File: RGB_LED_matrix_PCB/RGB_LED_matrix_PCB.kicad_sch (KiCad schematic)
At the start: 0 parts

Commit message: Routed the matrix structure
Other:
- added sheet LED_ROW (10_LED_row/10_LED_row.kicad_sch)
- added sheet LED_ROW1 (10_LED_row/10_LED_row.kicad_sch)
- added sheet LED_ROW2 (10_LED_row/10_LED_row.kicad_sch)
- added sheet LED_ROW3 (10_LED_row/10_LED_row.kicad_sch)
- added sheet LED_ROW4 (10_LED_row/10_LED_row.kicad_sch)
- added sheet LED_ROW5 (10_LED_row/10_LED_row.kicad_sch)
- added sheet LED_ROW6 (10_LED_row/10_LED_row.kicad_sch)
- added sheet LED_ROW7 (10_LED_row/10_LED_row.kicad_sch)
- added sheet LED_ROW8 (10_LED_row/10_LED_row.kicad_sch)
- added sheet LED_ROW9 (10_LED_row/10_LED_row.kicad_sch)

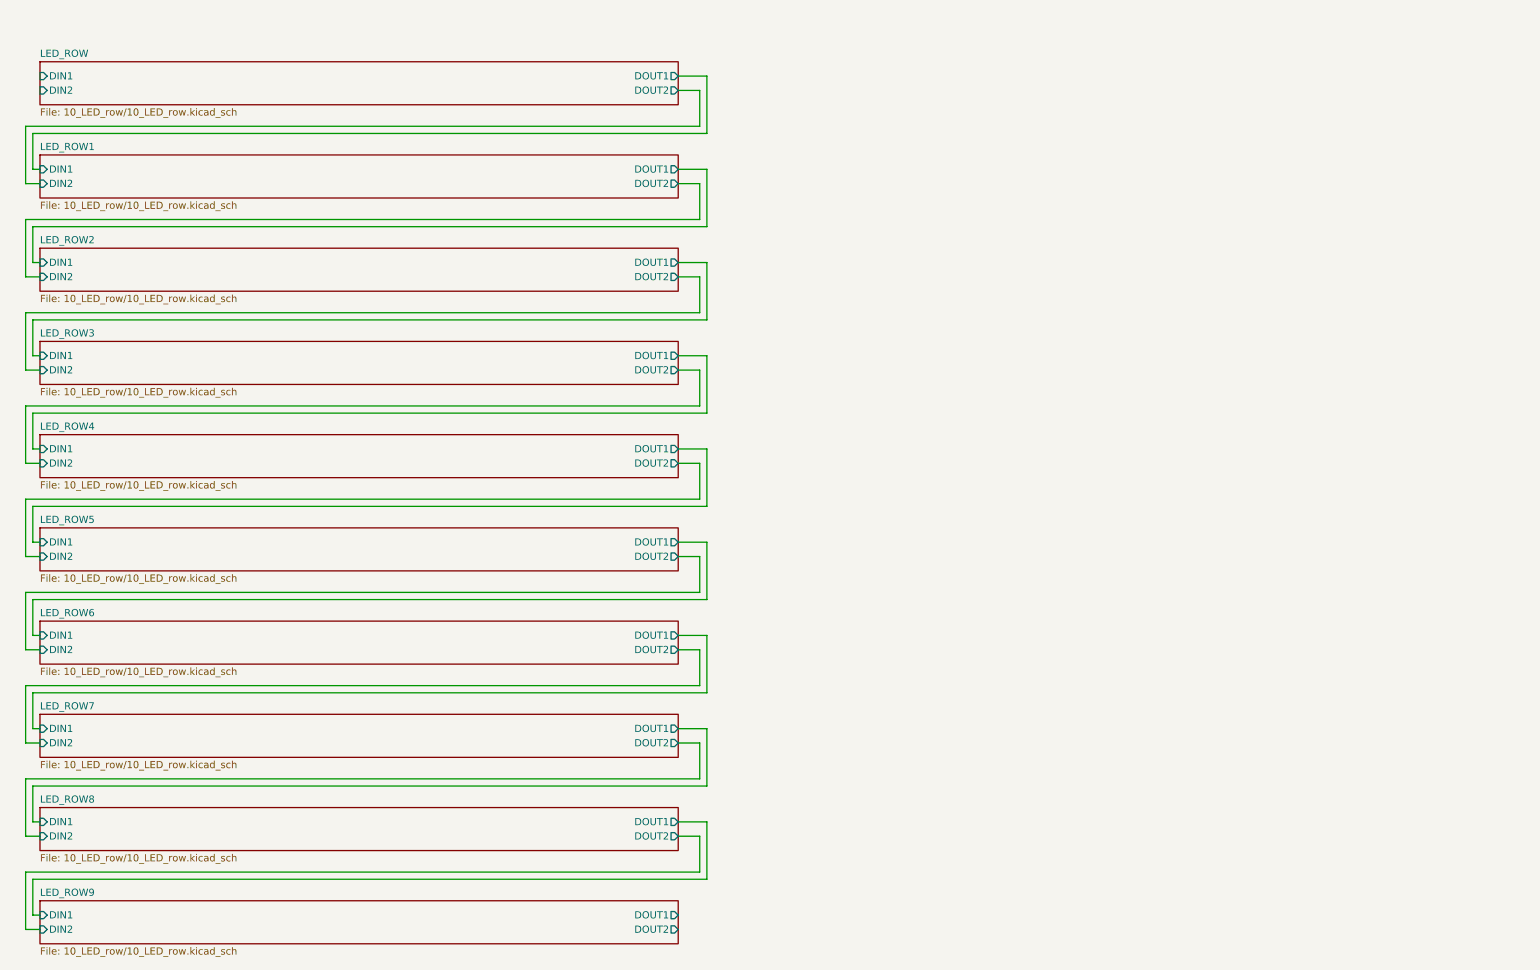
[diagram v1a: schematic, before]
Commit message: Changed LED matrix pcb design to a serpentine structure for better signal integrity. Proceeded with adding the connector and capacitors.
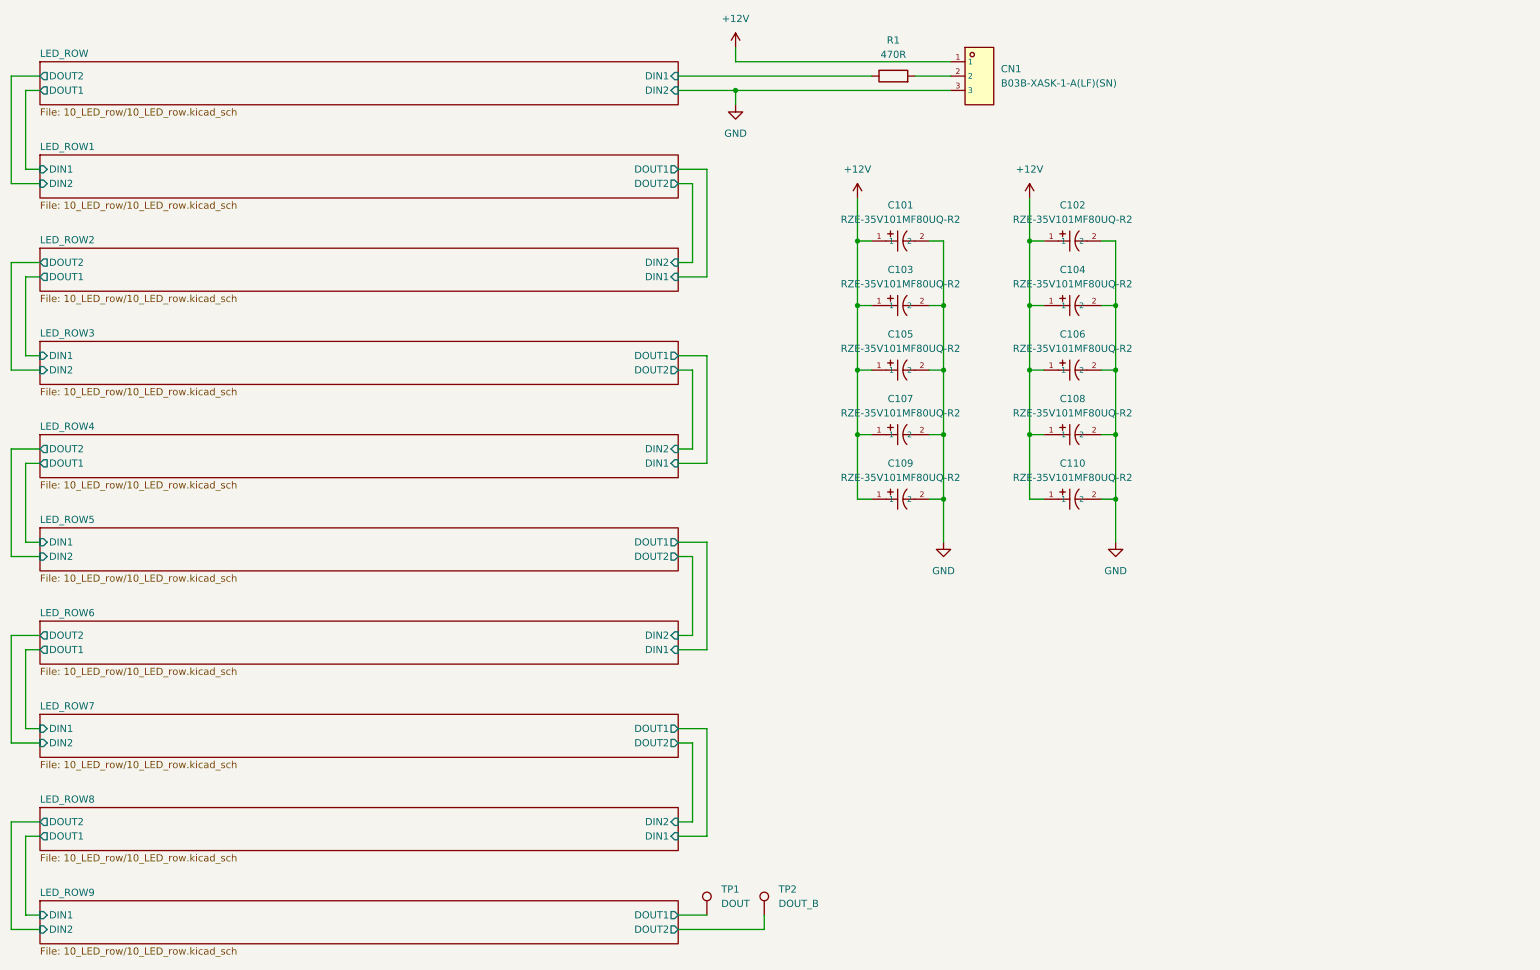
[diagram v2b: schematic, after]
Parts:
- added C101, C102, C103, C104, C105, C106, C107, C108, C109, C110: RZE-35V101MF80UQ-R2, lcsc_footprints:C19673858_CAP-SMD_BD6_3-L6_5-W6_5-LS7_2-FD_1, symbol lcsc_imported:RZE-35V101MF80UQ-R2
- added CN1: B03B-XASK-1-A(LF)(SN), lcsc_footprints:C264992_CONN-TH_B03B-XASK-1-A-LF-SN, symbol lcsc_imported:B03B-XASK-1-A(LF)(SN)
- added R1: 470R, Resistor_SMD:R_0402_1005Metric_Pad0.72x0.64mm_HandSolder, symbol Device:R
- added TP1: DOUT, TestPoint:TestPoint_Pad_D1.0mm, symbol Connector:TestPoint
- added TP2: DOUT_B, TestPoint:TestPoint_Pad_D1.0mm, symbol Connector:TestPoint
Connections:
- net LED_ROW/DIN1: now also R1.1
- net LED_ROW9/DOUT1: now also TP1.1
- net LED_ROW9/DOUT2: now also TP2.1
- new net: CN1.2, R1.2
- new net +12V: C101.1, C102.1, C103.1, C104.1, C105.1, C106.1, C107.1, C108.1, C109.1, C110.1, CN1.1
- new net GND: C101.2, C102.2, C103.2, C104.2, C105.2, C106.2, C107.2, C108.2, C109.2, C110.2, CN1.3

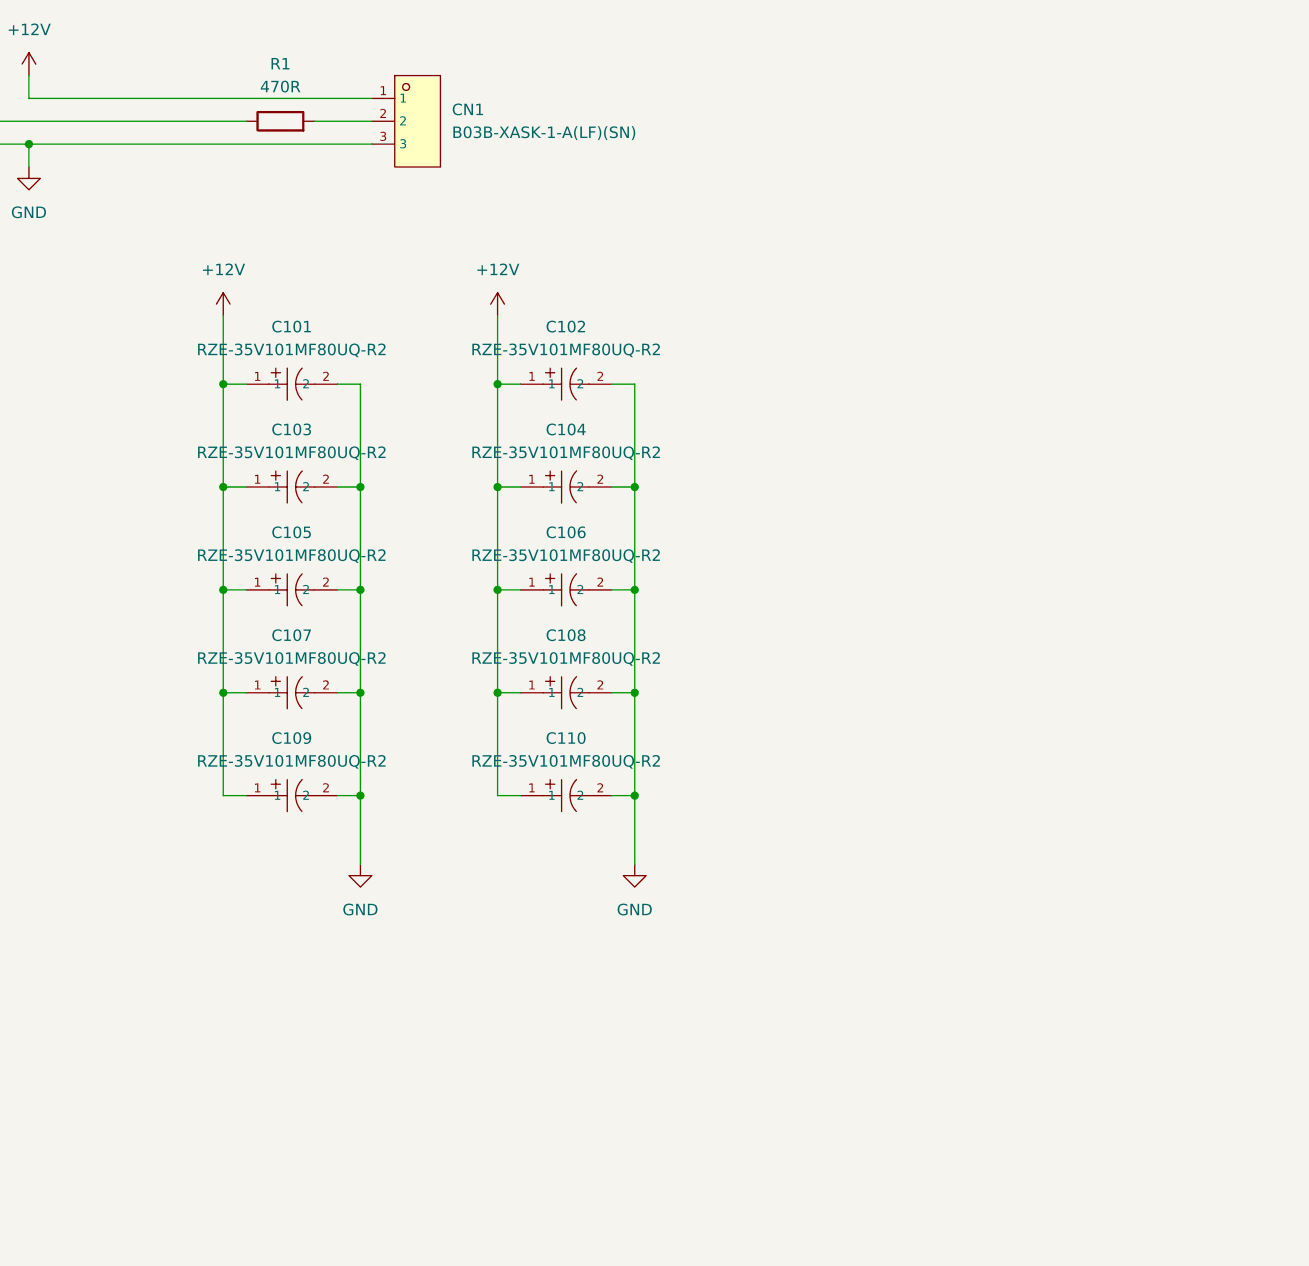
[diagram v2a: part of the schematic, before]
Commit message: Finished the LED matrix board layout - it just needs some polishing now and minor fixes
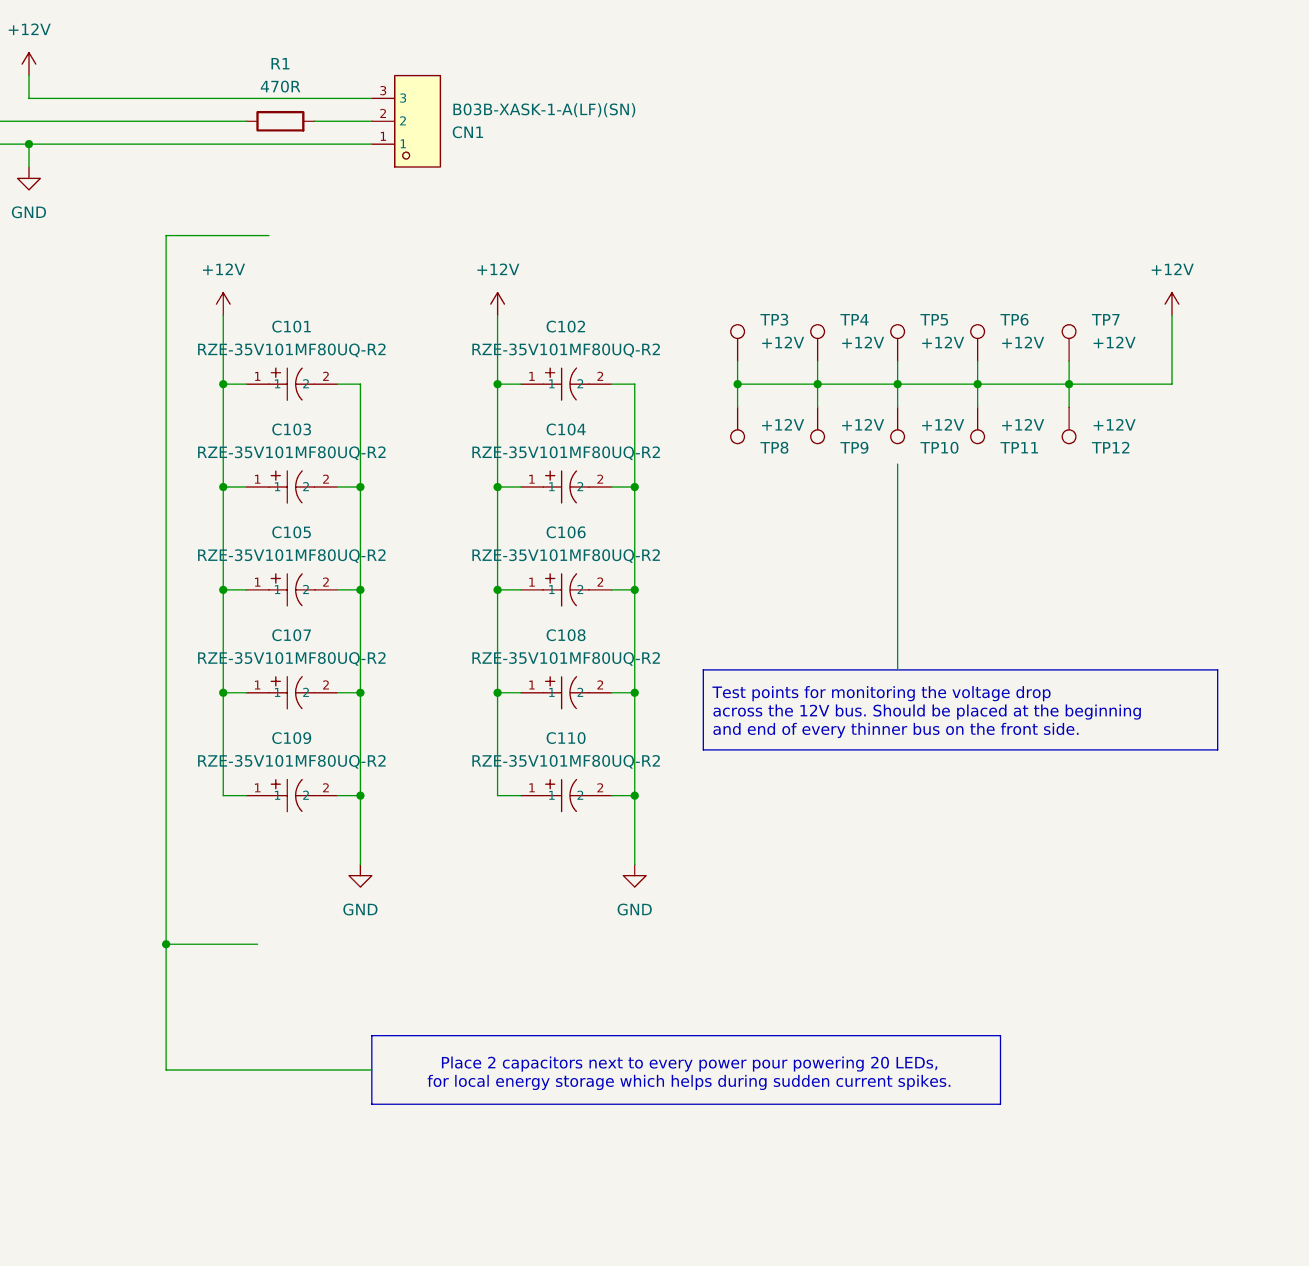
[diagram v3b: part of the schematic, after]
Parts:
- added TP10, TP11, TP12, TP3, TP4, TP5, TP6, TP7, TP8, TP9: +12V, TestPoint:TestPoint_Pad_D1.0mm, symbol Connector:TestPoint
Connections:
- net +12V: now also CN1.3, TP10.1, TP11.1, TP12.1, TP3.1, TP4.1, TP5.1, TP6.1, TP7.1, TP8.1, TP9.1; no longer CN1.1
- net GND: now also CN1.1; no longer CN1.3
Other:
- note added: "Place 2 capacitors next to every power pour powering 20 LEDs, for local energy storage which helps during sudden current spikes."
- note added: "Test points for monitoring the voltage drop across the 12V bus. Should be placed at the beginning and end of every thinner bus on the front side."
- title: (none) -> RGB LED MATRIX

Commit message: Made some slight modyfications to the RGB LED matrix layout.
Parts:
- added C111: RZE-35V101MF80UQ-R2, lcsc_footprints:C19673858_CAP-SMD_BD6_3-L6_5-W6_5-LS7_2-FD_1, symbol lcsc_imported:RZE-35V101MF80UQ-R2
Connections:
- net +12V: now also C111.1
- net GND: now also C111.2
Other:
- note added: "This is an alternate placement of the C101, mark as DNF if not needed."
- moved on the sheet: R1

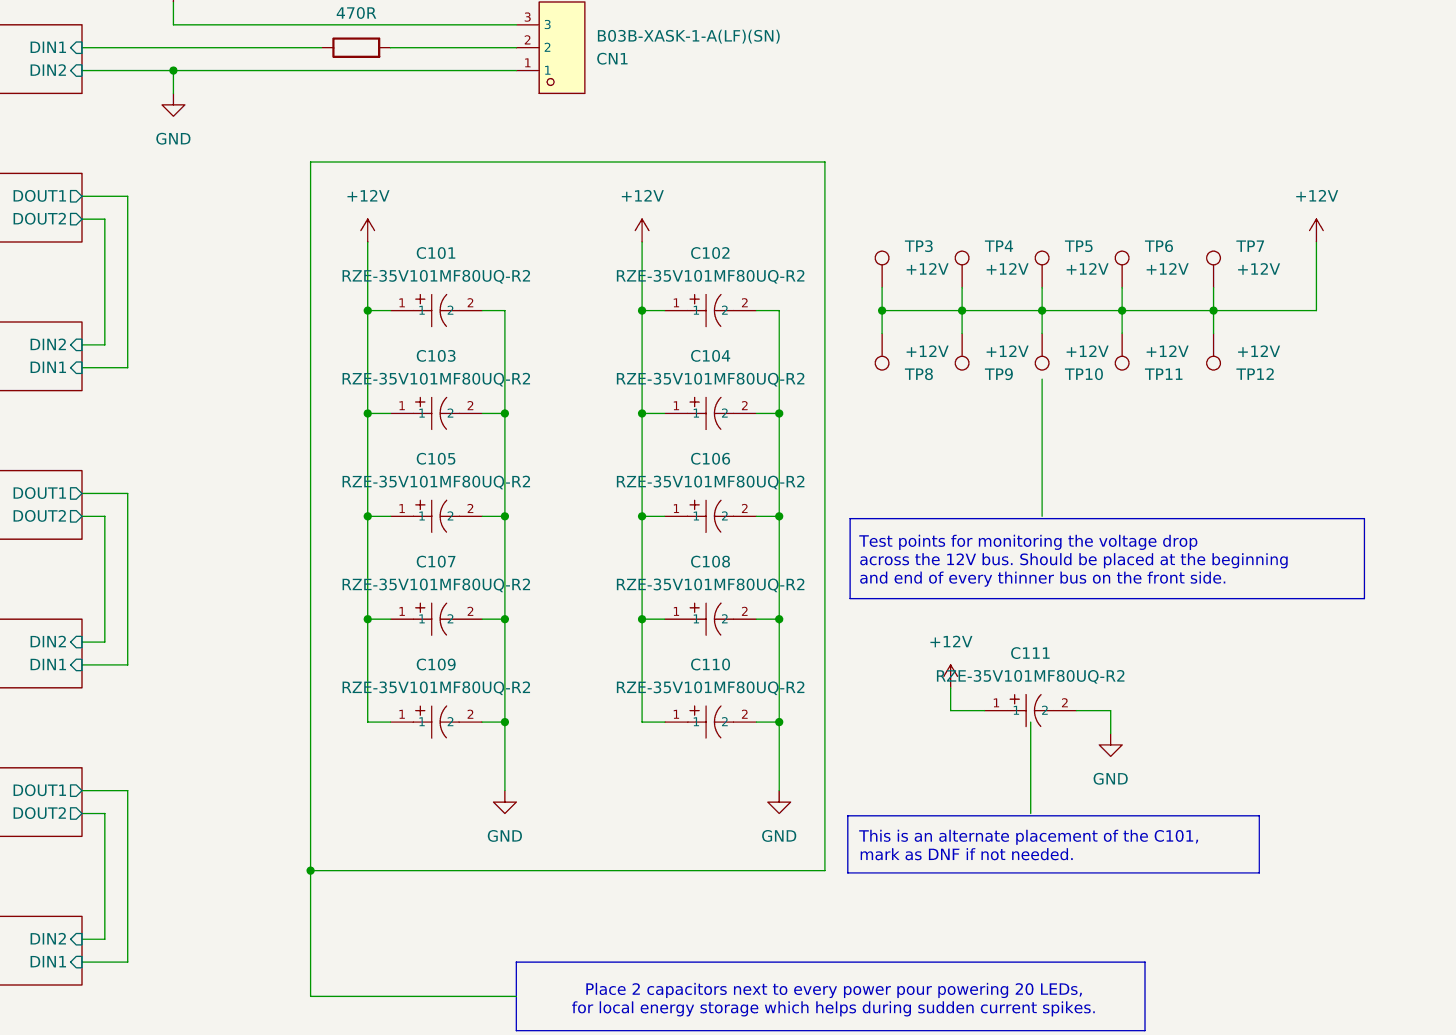
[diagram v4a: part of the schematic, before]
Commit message: Fixed silkscreen and added extra capacitor row in a new design variant in LED matrix PCB.
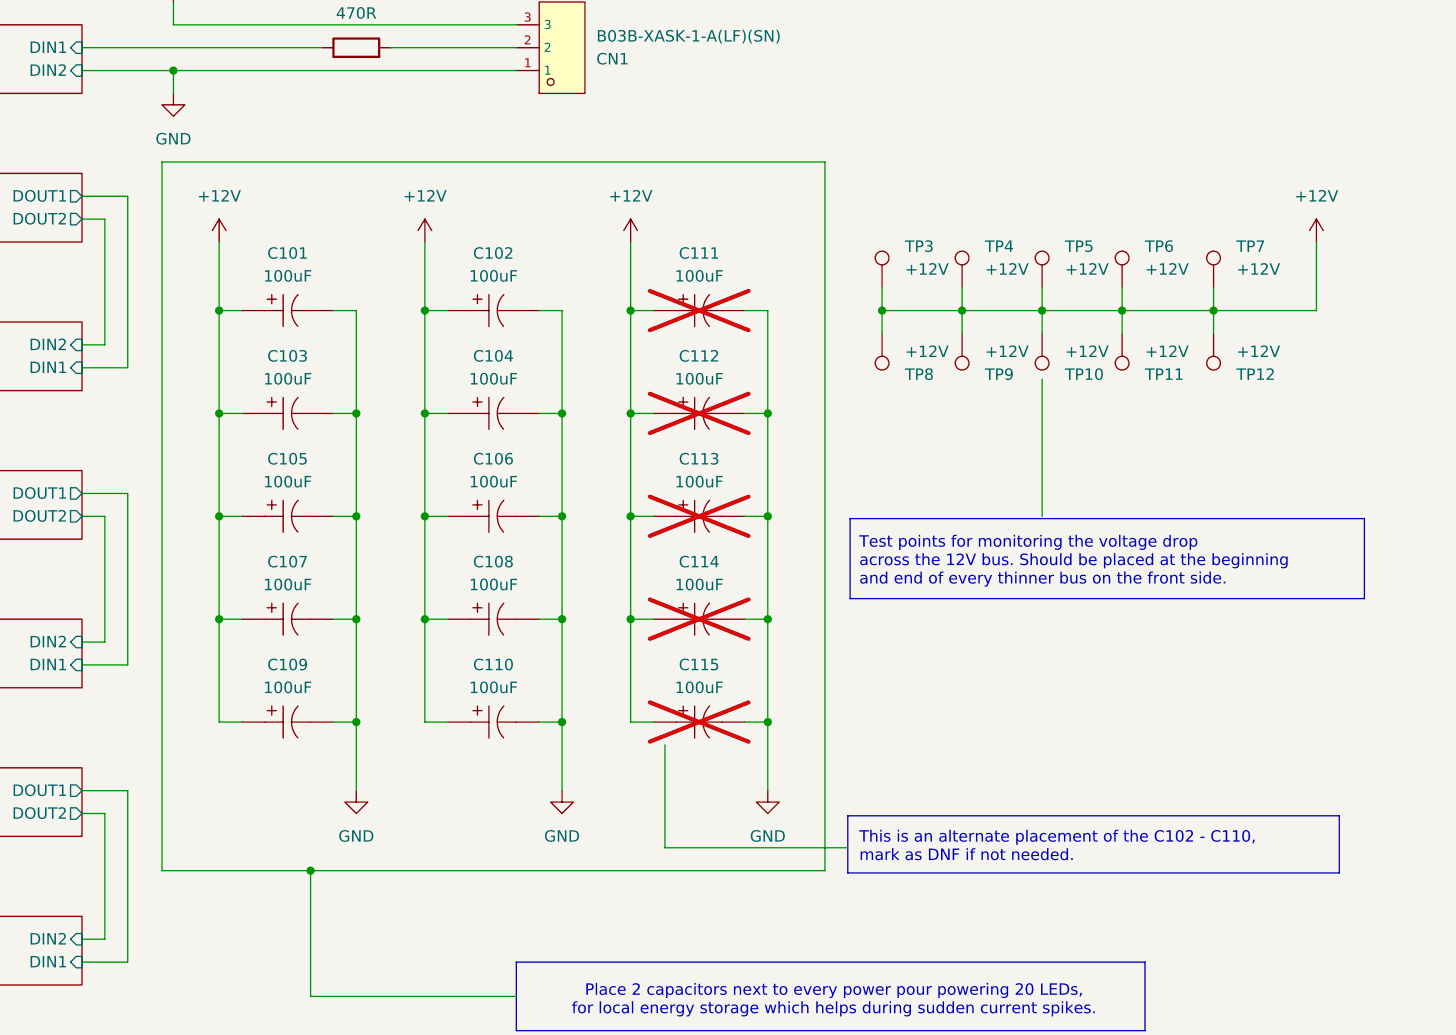
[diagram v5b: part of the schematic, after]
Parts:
- added C112, C113, C114, C115: 100uF, lcsc_footprints:C19673858_CAP-SMD_BD6_3-L6_5-W6_5-LS7_2-FD_1, symbol lcsc_imported:RZE-35V101MF80UQ-R2
- C101, C102, C103, C104, C105, C106, C107, C108, C109, C110: value RZE-35V101MF80UQ-R2 -> 100uF
- C111: value RZE-35V101MF80UQ-R2 -> 100uF; now not fitted
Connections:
- net +12V: now also C112.1, C113.1, C114.1, C115.1
- net GND: now also C112.2, C113.2, C114.2, C115.2
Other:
- note added: "This is an alternate placement of the C102 - C110, mark as DNF if not needed."
- note removed: "This is an alternate placement of the C101, mark as DNF if not needed."

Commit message: Forgot to add the LED matrix pcb to the last commit, same thing as with the UPDCB.
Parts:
- added H1, H2, H3, H4: MountingHole_Pad, MountingHole:MountingHole_2.2mm_M2_DIN965_Pad_TopOnly, symbol Mechanical:MountingHole_Pad
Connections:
- net GND: now also H1.1, H2.1, H3.1, H4.1
